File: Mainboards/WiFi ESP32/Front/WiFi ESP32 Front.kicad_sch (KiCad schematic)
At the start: 1 part

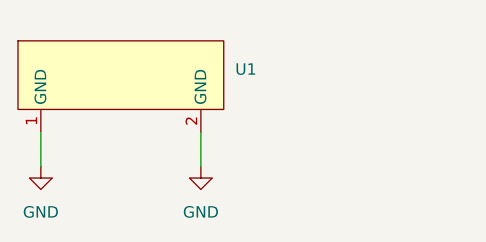
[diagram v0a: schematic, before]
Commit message: Migrate to new KiCad Version
Add SMA connector front
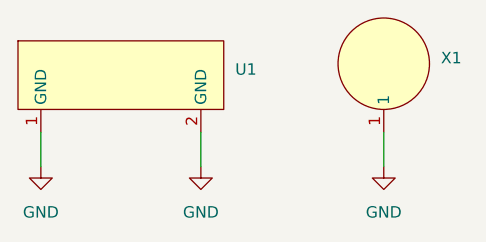
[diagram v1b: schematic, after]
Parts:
- added X1: ~, AllSerial:SMA-D, symbol AllSerial_Front:SMA-Hole
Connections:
- net GND: now also X1.1
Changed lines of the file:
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@@
+	(wire
+		(pts
+			(xy 143.51 90.17) (xy 143.51 93.98)
+		)
+		(stroke
+			(width 0)
+			(type default)
+		)
+	)
 	(wire
 		(pts
@@
 			(width 0)
 			(type default)
+		)
+	)
+	(symbol
+		(lib_id "power:GND")
+		(at 143.51 93.98 0)
+		(unit 1)
+		(exclude_from_sim no)
+		(in_bom yes)
+		(on_board yes)
+		(dnp no)
+		(fields_autoplaced yes)
+		(property "Reference" "#PWR03"
+			(at 143.51 100.33 0)
+			(effects
+				(font
+					(size 1.27 1.27)
+				)
+				(hide yes)
+			)
+		)
+		(property "Value" "GND"
+			(at 143.51 99.06 0)
+			(effects
+				(font
+					(size 1.27 1.27)
+				)
+			)
+		)
+		(property "Footprint" ""
+			(at 143.51 93.98 0)
+			(effects
+				(font
+					(size 1.27 1.27)
+				)
+				(hide yes)
+			)
+		)
+		(property "Datasheet" ""
+			(at 143.51 93.98 0)
+			(effects
+				(font
+					(size 1.27 1.27)
+				)
+				(hide yes)
+			)
+		)
+		(property "Description" "Power symbol creates a global label with name \"GND\" , ground"
+			(at 143.51 93.98 0)
+			(effects
+				(font
+					(size 1.27 1.27)
+				)
+				(hide yes)
+			)
+		)
+		(pin "1"
+		)
+		(instances
+			(project "WiFi ESP32 Front"
+				(path "/3a5d0197-32a1-4754-b306-0c3e0609959a"
+					(reference "#PWR03")
+					(unit 1)
+				)
+			)
 		)
 	)
@@
 					(unit 1)
 				)
+			)
+		)
+	)
+	(symbol
+		(lib_id "AllSerial_Front:SMA-Hole")
+		(at 143.51 87.63 0)
+		(unit 1)
+		(exclude_from_sim no)
+		(in_bom yes)
+		(on_board yes)
+		(dnp no)
+		(fields_autoplaced yes)
+		(property "Reference" "X1"
+			(at 149.86 81.9149 0)
+			(effects
+				(font
+					(size 1.27 1.27)
+				)
+				(justify left)
+			)
+		)
+		(property "Value" "~"
+			(at 149.86 83.82 0)
+			(effects
+				(font
+					(size 1.27 1.27)
+				)
+				(justify left)
+			)
+		)
+		(property "Footprint" "AllSerial:SMA-D"
+			(at 143.51 87.63 0)
+			(effects
+				(font
+					(size 1.27 1.27)
+				)
+				(hide yes)
+			)
+		)
+		(property "Datasheet" ""
+			(at 143.51 87.63 0)
+			(effects
+				(font
+					(size 1.27 1.27)
+				)
+				(hide yes)
+			)
+		)
+		(property "Description" ""
+			(at 143.51 87.63 0)
+			(effects
+				(font
+					(size 1.27 1.27)
+				)
+				(hide yes)
+			)
+		)
+		(pin "1"
+		)
+		(instances
+			(project ""
+				(path "/3a5d0197-32a1-4754-b306-0c3e0609959a"
+					(reference "X1")
+					(unit 1)
+				)
